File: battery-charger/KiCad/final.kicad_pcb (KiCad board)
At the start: 2 copper layers, 99.6 x 22.7 mm, 21 parts, among them Q1 MOSFET_P, SW1 SPST, U1 BQ2057W

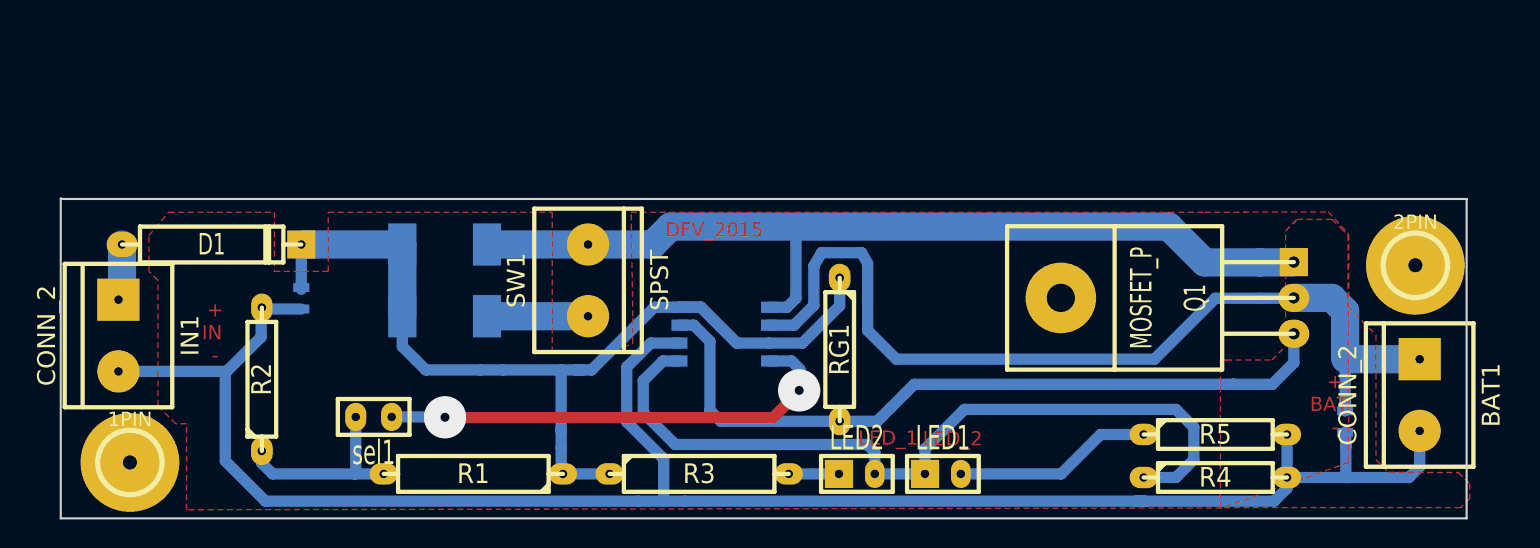
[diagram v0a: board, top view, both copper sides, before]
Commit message: Link correctly the specific footprint library and change one component
The two connectors are repleaced by a 3-pin connector in order to reduce
length of power traces.
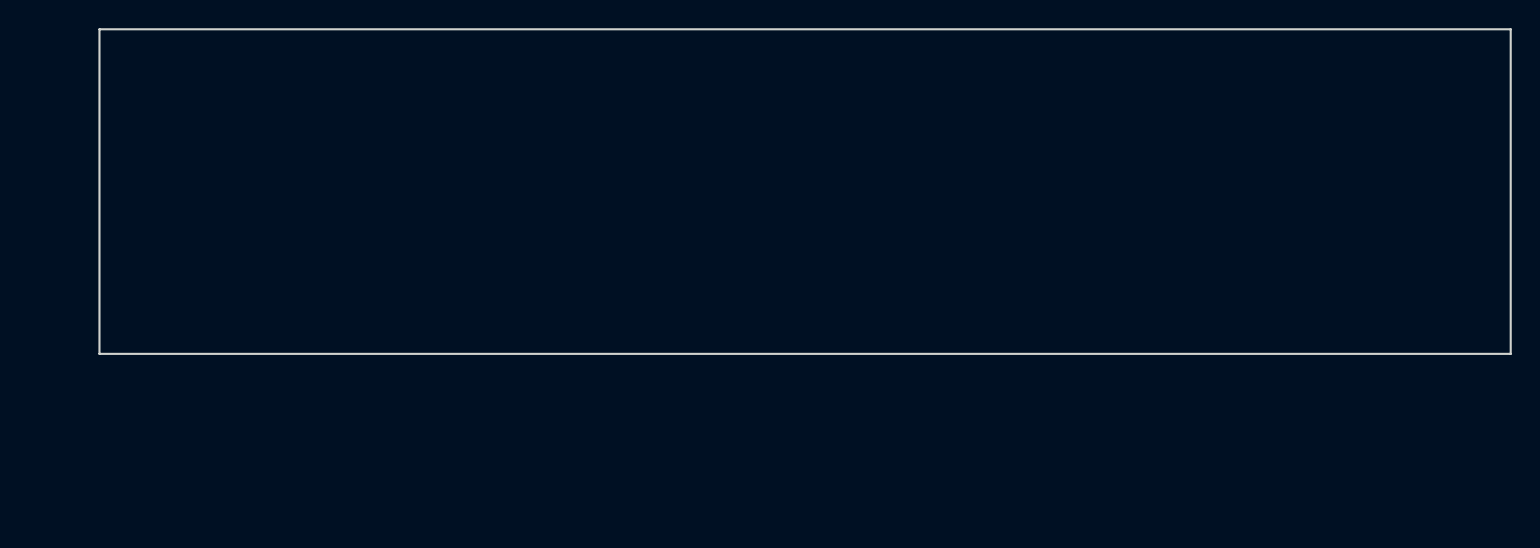
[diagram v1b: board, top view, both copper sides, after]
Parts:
- removed 1PIN, 2PIN: P***, 1pin
- removed BAT1, IN1: CONN_2, bornier2
- removed C1, C2: 0.1uF, SM0603
- removed D1: DIODESCH, D5
- removed LED1, LED2, sel1: CONN_2, SIL-2
- removed Q1: MOSFET_P, TO220GDS
- removed R1: 10k, R5
- removed R2: 10k, R4
- removed R3: 511, R5
- removed R4, R5, RG1: 1k, R4
- removed Rsns1: 0.12, SM2512
- removed Rsns2: 0.15, SM2512
- removed SW1: SPST, bornier2
- removed U1: BQ2057W, SO8N
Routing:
- net N-0000012: track 134.6 -> 0.00 mm
- net N-000004: track 72.6 -> 0.00 mm
- net N-000002: track 65.8 -> 0.00 mm
- net N-000009: track 65.7 -> 0.00 mm
- net N-000003: track 57.0 -> 0.00 mm
- net N-0000010: track 53.2 -> 0.00 mm
- net N-000001: track 33.7 -> 0.00 mm, vias 2 -> 0
- net N-000008: track 14.1 -> 0.00 mm
- net N-000007: track 13.9 -> 0.00 mm
- net N-000006: track 6.98 -> 0.00 mm
- net N-000005: track 4.02 -> 0.00 mm
- net N-0000011: track 3.56 -> 0.00 mm
- removed copper zone on F.Cu, net (none)
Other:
- board size 99.6 x 22.7 mm -> 100 x 23 mm
- board text removed: "+ BAT -"
- board text removed: "+ IN -"
- board text removed: "DFV_2015"
- board text removed: "LED_1"
- board text removed: "LED_2"

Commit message: Update the v2.0 of the battery charger PCB
Include the Bill of Materials (BOM) with all the components

Include all the footprints in the footprint library
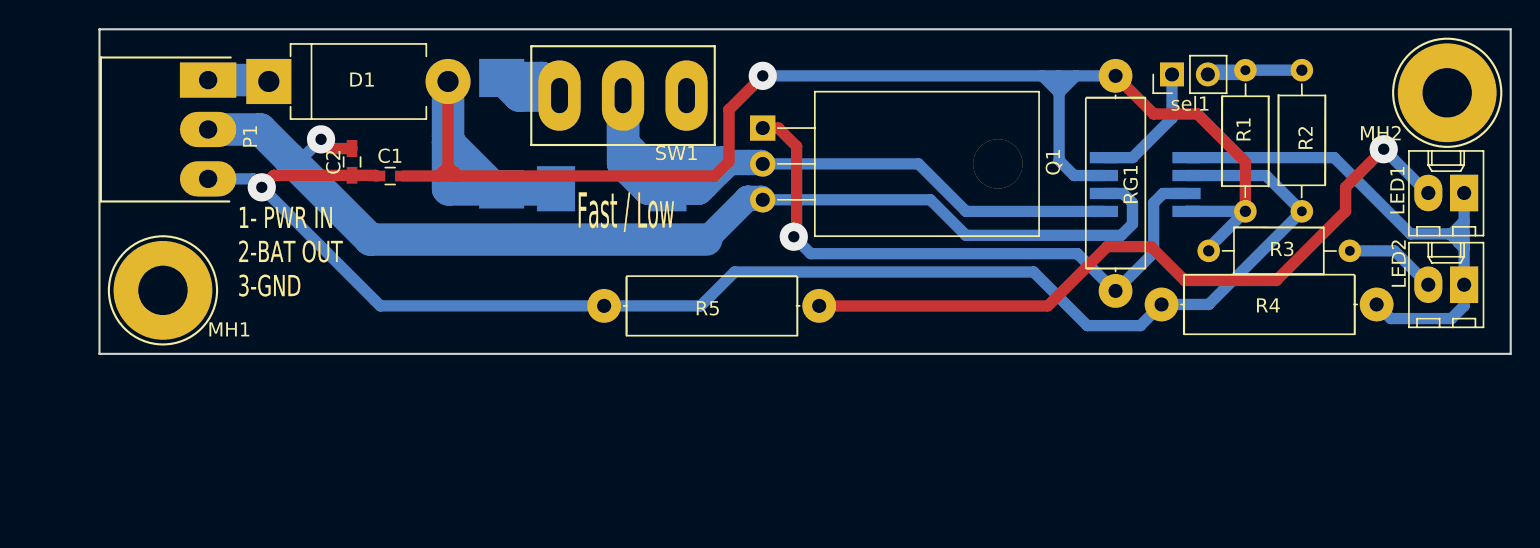
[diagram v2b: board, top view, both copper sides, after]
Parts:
- added C1: 0.1uF, footprint:C_0603, F.Cu at (120.6, 90.4)
- added C2: 0.1uF, footprint:C_0603, F.Cu at (117.9, 89.4)
- added D1: DIODESCH, footprint:D_DO-201AD, F.Cu at (112.0, 83.7)
- added LED1: CONN_2, footprint:Molex_02x01, F.Cu at (196.7, 91.6)
- added LED2: CONN_2, footprint:Molex_02x01, F.Cu at (196.7, 98.1)
- added MH1: Mounting_Hole, footprint:Mounting_hole, F.Cu at (104.5, 98.5)
- added MH2: Mounting_Hole, footprint:Mounting_hole, F.Cu at (195.5, 84.5)
- added P1: CONN_01X03, footprint:Molex_03x01_Straight, F.Cu at (104.7, 86.6)
- added Q1: MOSFET_P, footprint:TO-220-3, F.Cu at (147.0, 87.0)
- added R1: 10k, footprint:R_THT_0.54, F.Cu at (181.2, 92.9)
- added R2: 10k, footprint:R_THT_0.54, F.Cu at (185.2, 82.9)
- added R3: 511, footprint:R_THT_0.54, F.Cu at (178.6, 95.7)
- added R4: 1k, footprint:R_THT_0.78, F.Cu at (190.5, 99.5)
- added R5: 1k, footprint:R_THT_0.78, F.Cu at (151.0, 99.6)
- added RG1: 1k, footprint:R_THT_0.78, F.Cu at (172.0, 83.3)
- added Rsns1: 0.12, footprint:R_2512_HandSoldering, B.Cu at (128.5, 87.4)
- added Rsns2: 0.15, footprint:R_2512_HandSoldering, B.Cu at (136.3, 91.3)
- added SW1: SPST, footprint:Switch, F.Cu at (132.6, 84.7)
- added U1: BQ2057W, footprint:SOIC-8_Handsoldering, B.Cu at (174.1, 91.0)
- added sel1: CONN_2, footprint:Pin_Header_Straight_01x02, F.Cu at (176.0, 83.2)
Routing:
- net Net-(C1-Pad1): track 0.00 -> 120.9 mm, vias 0 -> 1
- net /GND: track 0.00 -> 104.9 mm, vias 0 -> 1
- net /BAT_OUT: track 0.00 -> 80.5 mm, vias 0 -> 1
- net Net-(Q1-PadS): track 0.00 -> 65.9 mm
- net Net-(LED1-Pad2): track 0.00 -> 52.0 mm, vias 0 -> 1
- net Net-(Q1-PadG): track 0.00 -> 43.8 mm, vias 0 -> 1
- net Net-(LED1-Pad1): track 0.00 -> 40.7 mm
- net Net-(R1-Pad2): track 0.00 -> 9.57 mm
- net Net-(Rsns1-Pad2): track 0.00 -> 9.24 mm
- net Net-(U1-Pad4): track 0.00 -> 9.08 mm
- net Net-(LED2-Pad2): track 0.00 -> 6.55 mm
- net /PWR_IN: track 0.00 -> 4.34 mm
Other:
- board text added: "1- PWR IN 2-BAT OUT 3-GND"
- board text added: "Fast / Low"

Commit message: Prepare Silk Layer in order to be able to manufacture
This 'manu2' branch was created in order to have the 3 projects
on the same folder.

The silk layer was created and adapted to give it to an external
manufacturer.
Nearly the same information was created in the copper layer in order to
have this information also in the case the PCB's were manufactured in
the DTE.
The Mask layer was also adapted to give it to the external manufacturer.
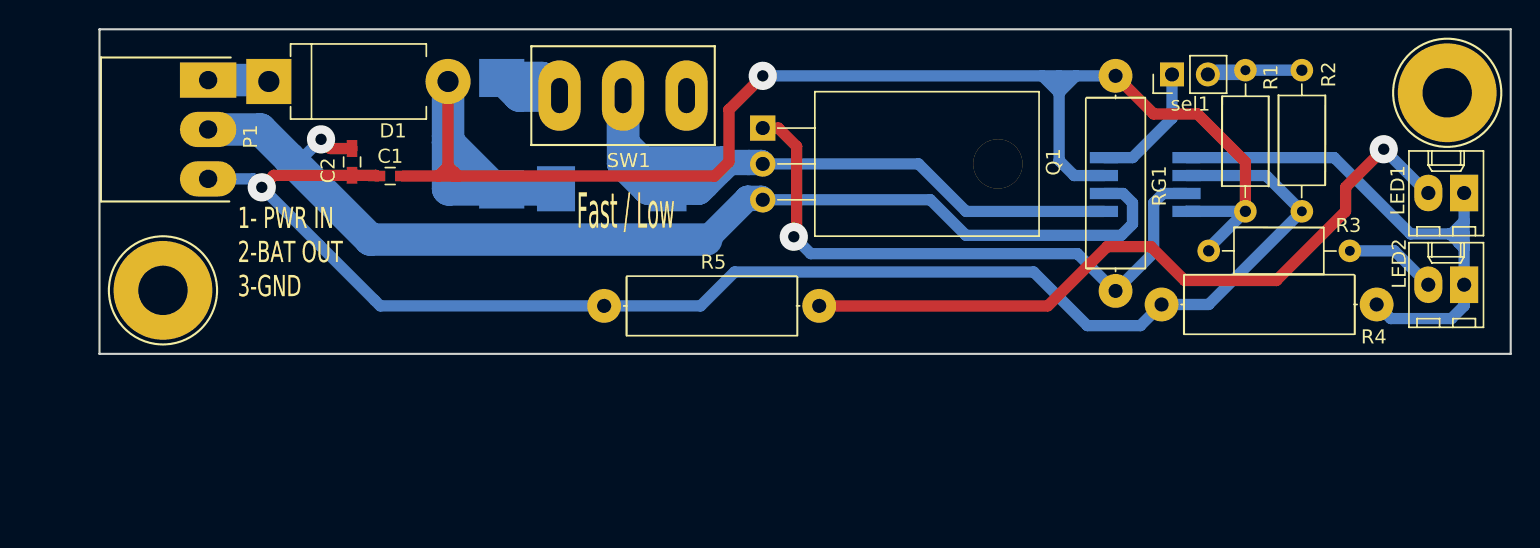
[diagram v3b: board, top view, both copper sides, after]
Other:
- rule pad_to_mask_clearance: 0 -> 0.1
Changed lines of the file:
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@@
     (37 F.SilkS user)
     (38 B.Mask user hide)
-    (39 F.Mask user hide)
+    (39 F.Mask user)
     (40 Dwgs.User user hide)
     (41 Cmts.User user hide)
@@
     (pad_size 3 3)
     (pad_drill 0.6)
-    (pad_to_mask_clearance 0)
+    (pad_to_mask_clearance 0.1)
     (aux_axis_origin 0 0)
-    (visible_elements 7FFEDEE9)
+    (visible_elements 7FFEDE69)
     (pcbplotparams
-      (layerselection 0x00030_80000001)
-      (usegerberextensions false)
-      (excludeedgelayer false)
+      (layerselection 0x010e0_80000001)
+      (usegerberextensions true)
+      (excludeedgelayer true)
       (linewidth 0.150000)
-      (plotframeref true)
+      (plotframeref false)
       (viasonmask false)
       (mode 1)
@@
       (psa4output false)
       (plotreference true)
-      (plotvalue true)
+      (plotvalue false)
       (plotinvisibletext false)
-      (padsonsilk true)
+      (padsonsilk false)
       (subtractmaskfromsilk false)
-      (outputformat 4)
+      (outputformat 1)
       (mirror false)
-      (drillshape 2)
+      (drillshape 0)
       (scaleselection 1)
-      (outputdirectory FabricationOutputs/))
+      (outputdirectory C:/GIT/GERBER/battery-charger/))
   )
   (net 0 "")
@@
     (tags "capacitor 0603")
     (attr smd)
-    (fp_text reference C2 (at 0 1.3 450) (layer F.SilkS)
+    (fp_text reference C2 (at 0.6 1.7 450) (layer F.SilkS)
       (effects (font (size 1 1) (thickness 0.15)))
     )
@@
     (descr "Resistor, Axial_DIN0309 series, Axial, Horizontal, pin pitch=12.7mm, 0.5W = 1/2W, length*diameter=9*3.2mm^2, http://cdn-reichelt.de/documents/datenblatt/B400/1_4W%23YAG.pdf")
     (tags "Resistor Axial_DIN0309 series Axial Horizontal pin pitch 12.7mm 0.5W = 1/2W length 9mm diameter 3.2mm")
-    (fp_text reference R1 (at 5.8 -0.1 90) (layer F.SilkS)
+    (fp_text reference R1 (at 9.5 1.8 90) (layer F.SilkS)
       (effects (font (size 1 1) (thickness 0.15)))
     )
@@
     (descr "Resistor, Axial_DIN0309 series, Axial, Horizontal, pin pitch=12.7mm, 0.5W = 1/2W, length*diameter=9*3.2mm^2, http://cdn-reichelt.de/documents/datenblatt/B400/1_4W%23YAG.pdf")
     (tags "Resistor Axial_DIN0309 series Axial Horizontal pin pitch 12.7mm 0.5W = 1/2W length 9mm diameter 3.2mm")
-    (fp_text reference R2 (at 4.8 -0.3 270) (layer F.SilkS)
+    (fp_text reference R2 (at 0.3 -1.9 270) (layer F.SilkS)
       (effects (font (size 1 1) (thickness 0.15)))
     )
@@
     (descr "Resistor, Axial_DIN0309 series, Axial, Horizontal, pin pitch=12.7mm, 0.5W = 1/2W, length*diameter=9*3.2mm^2, http://cdn-reichelt.de/documents/datenblatt/B400/1_4W%23YAG.pdf")
     (tags "Resistor Axial_DIN0309 series Axial Horizontal pin pitch 12.7mm 0.5W = 1/2W length 9mm diameter 3.2mm")
-    (fp_text reference R3 (at 5.2 -0.1) (layer F.SilkS)
+    (fp_text reference R3 (at 9.9 -1.8) (layer F.SilkS)
       (effects (font (size 1 1) (thickness 0.15)))
     )
@@
     (descr "Resistor, Axial_DIN0414 series, Axial, Horizontal, pin pitch=15.24mm, 2W, length*diameter=11.9*4.5mm^2, http://www.vishay.com/docs/20128/wkxwrx.pdf")
     (tags "Resistor Axial_DIN0414 series Axial Horizontal pin pitch 15.24mm 2W length 11.9mm diameter 4.5mm")
-    (fp_text reference R4 (at 7.7 -0.1 180) (layer F.SilkS)
+    (fp_text reference R4 (at 0.2 -2.3 180) (layer F.SilkS)
       (effects (font (size 1 1) (thickness 0.15)))
     )
@@
     (descr "Resistor, Axial_DIN0414 series, Axial, Horizontal, pin pitch=15.24mm, 2W, length*diameter=11.9*4.5mm^2, http://www.vishay.com/docs/20128/wkxwrx.pdf")
     (tags "Resistor Axial_DIN0414 series Axial Horizontal pin pitch 15.24mm 2W length 11.9mm diameter 4.5mm")
-    (fp_text reference R5 (at 7.9 -0.2 180) (layer F.SilkS)
+    (fp_text reference R5 (at 7.5 3.1 180) (layer F.SilkS)
       (effects (font (size 1 1) (thickness 0.15)))
     )
@@
     (descr "Resistor, Axial_DIN0414 series, Axial, Horizontal, pin pitch=15.24mm, 2W, length*diameter=11.9*4.5mm^2, http://www.vishay.com/docs/20128/wkxwrx.pdf")
     (tags "Resistor Axial_DIN0414 series Axial Horizontal pin pitch 15.24mm 2W length 11.9mm diameter 4.5mm")
-    (fp_text reference RG1 (at 7.7 -1.1 270) (layer F.SilkS)
+    (fp_text reference RG1 (at 7.8 -3.1 270) (layer F.SilkS)
       (effects (font (size 1 1) (thickness 0.15)))
     )
@@
     (tags "resistor 2512")
     (attr smd)
-    (fp_text reference Rsns2 (at 0 -2.5) (layer B.SilkS)
+    (fp_text reference Rsns2 (at 0.4 -2.5) (layer B.SilkS)
       (effects (font (size 1 1) (thickness 0.15)) (justify mirror))
     )
@@
     (at 132.6 84.7)
     (descr "WireConnection with 2.5mm drill")
-    (fp_text reference SW1 (at 8.3 4.1) (layer F.SilkS)
+    (fp_text reference SW1 (at 4.9 4.6) (layer F.SilkS)
       (effects (font (size 1 1) (thickness 0.15)))
     )
@@
     (descr "D, DO-201AD series, Axial, Horizontal, pin pitch=12.7mm, , length*diameter=9.5*5.2mm^2, , http://www.diodes.com/_files/packages/DO-201AD.pdf")
     (tags "D DO-201AD series Axial Horizontal pin pitch 12.7mm  length 9.5mm diameter 5.2mm")
-    (fp_text reference D1 (at 6.6 -0.1) (layer F.SilkS)
+    (fp_text reference D1 (at 8.8 3.5) (layer F.SilkS)
       (effects (font (size 1 1) (thickness 0.15)))
     )
@@
     (descr "BNC connector")
     (tags "BNC connector")
-    (fp_text reference MH1 (at 4.7 2.8) (layer F.SilkS)
+    (fp_text reference MH1 (at 4.9 2.7) (layer F.SilkS) hide
       (effects (font (size 1 1) (thickness 0.15)))
     )
@@
     (descr "BNC connector")
     (tags "BNC connector")
-    (fp_text reference MH2 (at -4.7 2.9) (layer F.SilkS)
+    (fp_text reference MH2 (at -4.7 2.9) (layer F.SilkS) hide
       (effects (font (size 1 1) (thickness 0.15)))
     )
@@
   (segment (start 124.75 91.35) (end 124.7 91.3) (width 2.3) (layer B.Cu) (net 1))
   (segment (start 124.7 83.7) (end 124.7 87.55) (width 2.3) (layer B.Cu) (net 1))
-  (segment (start 117.9 90.35) (end 112.35 90.35) (width 0.8) (layer F.Cu) (net 2) (status 400000))
+  (segment (start 117.9 90.35) (end 112.35 90.35) (width 0.8) (layer F.Cu) (net 2))
   (via (at 111.5 91.2) (size 2) (drill 0.8) (layers F.Cu B.Cu) (net 2))
   (segment (start 112.35 90.35) (end 111.5 91.2) (width 0.8) (layer F.Cu) (net 2))
